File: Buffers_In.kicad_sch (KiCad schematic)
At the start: 19 parts, among them U3 MCP6002-xSN, X1 PEDAL_COMBO_TOP

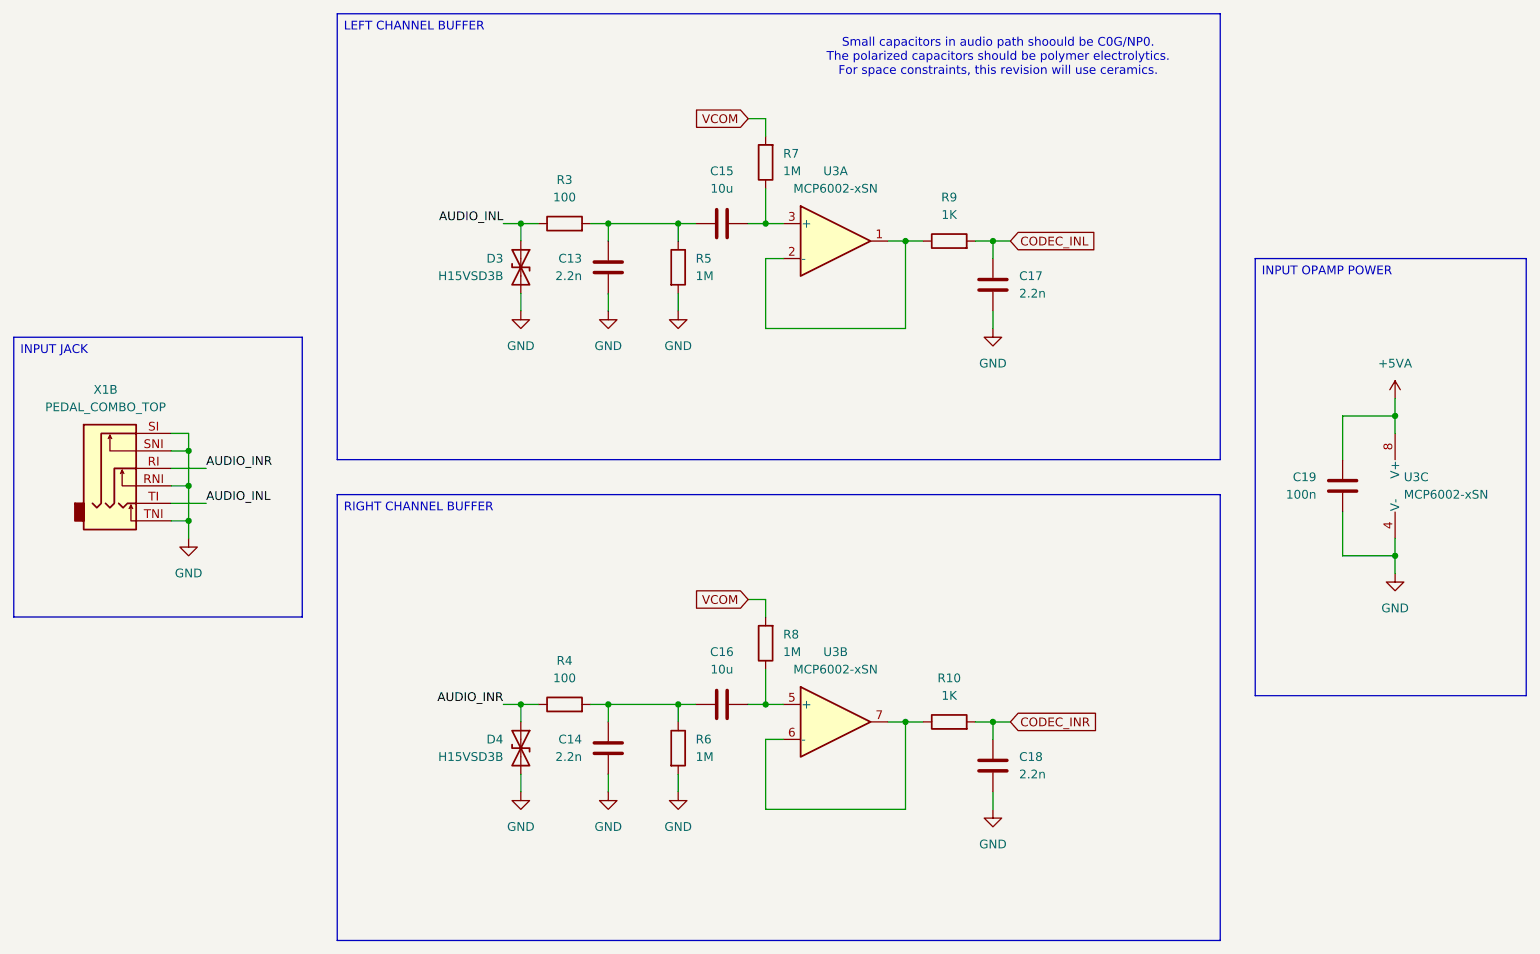
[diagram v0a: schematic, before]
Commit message: Input buffer and power
Updated the input buffer layout.
Updated the power supply layout.
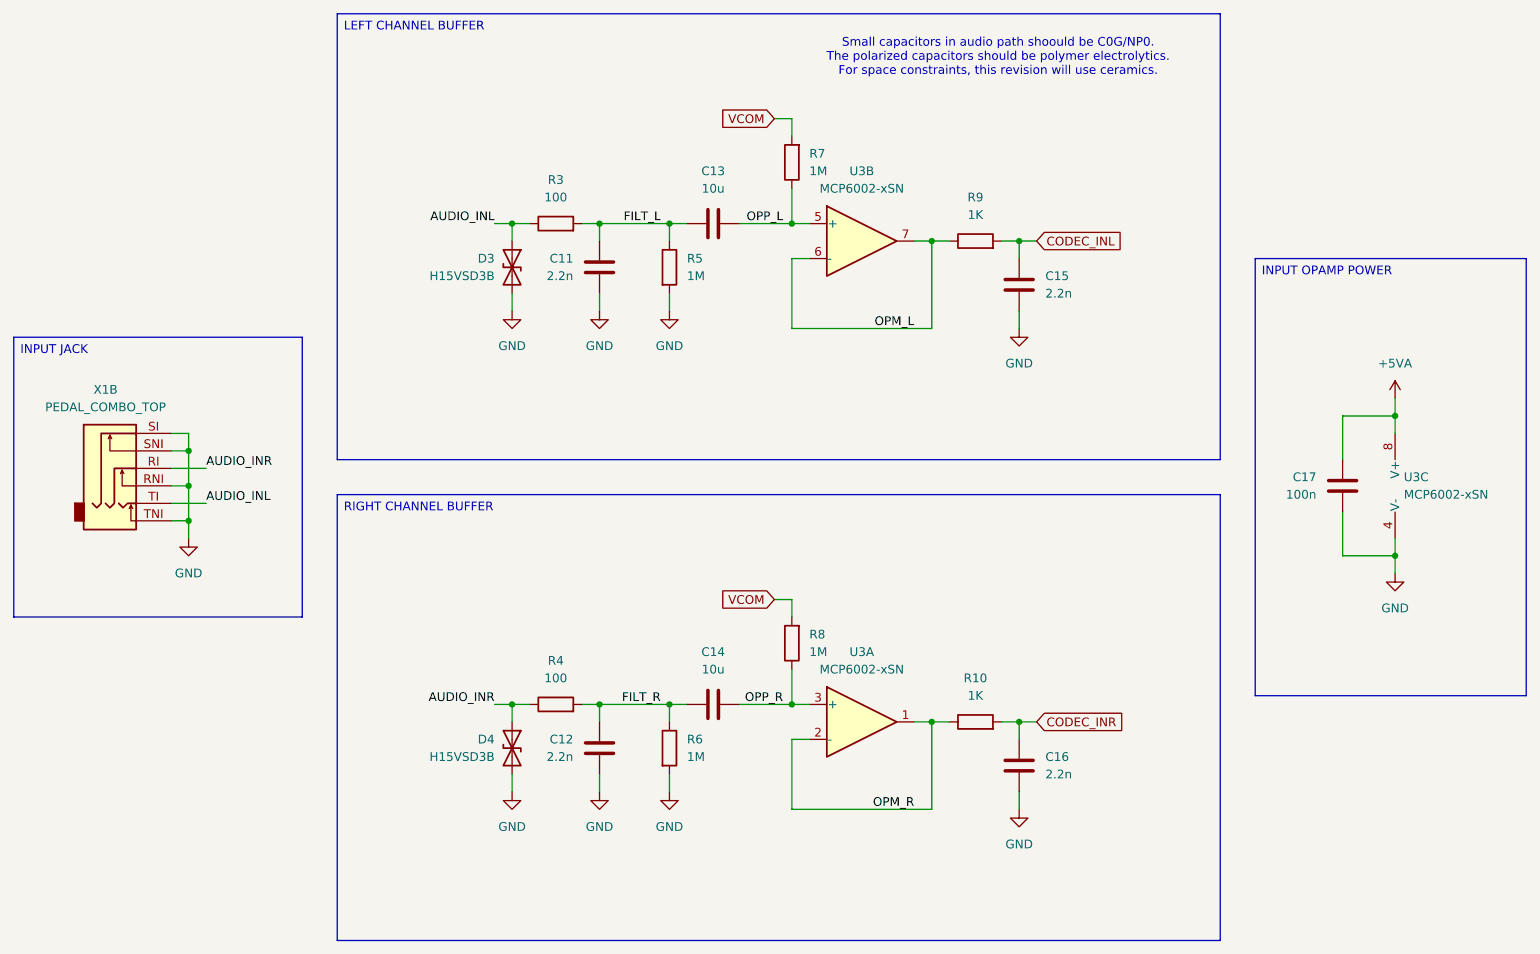
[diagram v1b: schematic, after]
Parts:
- C13: renamed from C15; footprint Capacitor_SMD:C_1206_3216Metric -> Capacitor_SMD:C_0805_2012Metric
- C14: renamed from C16; footprint Capacitor_SMD:C_1206_3216Metric -> Capacitor_SMD:C_0805_2012Metric
- renumbered C13 to C11, C14 to C12, C17 to C15, C18 to C16, C19 to C17
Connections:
- net FILT_R: now reaches C12.2, C14.1, R4.2, R6.1
- net OPM_L: now reaches U3.6 (-), U3.7
- net OPM_L: now also R9.1; no longer R10.1
- net OPM_R: now reaches U3.1, U3.2 (-)
- net OPM_R: now also R10.1; no longer R9.1
- net OPP_L: now reaches C13.2, R7.1
- net OPP_L: now also U3.5 (+); no longer U3.3 (+)
- net FILT_L: now reaches C11.2, C13.1, R3.2, R5.1
- net OPP_R: now reaches C14.2, R8.1
- net OPP_R: now also U3.3 (+); no longer U3.5 (+)
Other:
- moved on the sheet: C11, C12, C13, C14, C15, C16, D3, D4, R10, R3, R4, R5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

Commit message: Codec layout
Updated the codec layout.
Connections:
- net AUDIO_INL: now also R4.1; no longer R3.1
- net AUDIO_INR: now also R3.1; no longer R4.1
- net CODEC_INL: now also C16.1, R10.2; no longer C15.1, R9.2
- net CODEC_INR: now also C15.1, R9.2; no longer C16.1, R10.2
- net FILT_L: now also C12.2, C14.1, R4.2, R6.1; no longer C11.2, C13.1, R3.2, R5.1
- net FILT_R: now also C11.2, C13.1, R3.2, R5.1; no longer C12.2, C14.1, R4.2, R6.1
- net OPM_L: now also R10.1, U3.1, U3.2 (-); no longer R9.1, U3.6 (-), U3.7
- net OPM_R: now also R9.1, U3.6 (-), U3.7; no longer R10.1, U3.1, U3.2 (-)
- net OPP_L: now also C14.2, R8.1, U3.3 (+); no longer C13.2, R7.1, U3.5 (+)
- net OPP_R: now also C13.2, R7.1, U3.5 (+); no longer C14.2, R8.1, U3.3 (+)
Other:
- moved on the sheet: C11, C12, C13, C14, C15, C16, R10, R3, R4, R5, R6, R7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

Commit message: Missing connections
Updated the board layout.
Added al missing connections.
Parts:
- renumbered C12 to C11, C11 to C12, C14 to C13, C13 to C14, C16 to C15, C15 to C16, R9 to R10, R4 to R3, R3 to R4, R6 to R5, R5 to R6, R8 to R7, R7 to R8, R10 to R9
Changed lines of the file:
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@@
 		(on_board yes)
 		(dnp no)
-		(property "Reference" "C12"
+		(property "Reference" "C11"
 			(at 118.11 57.1501 0)
 			(effects
@@
 			(project "SimpleCodec"
 				(path "/4cbf131b-42e8-4a05-beea-68c6d66cdb1a/469e8ad1-854f-4ea5-8b66-be90c8cb100f"
-					(reference "C12")
+					(reference "C11")
 					(unit 1)
 				)
@@
 		(dnp no)
 		(fields_autoplaced yes)
-		(property "Reference" "R10"
+		(property "Reference" "R9"
 			(at 176.53 48.26 90)
 			(effects
@@
 			(project "SimpleCodec"
 				(path "/4cbf131b-42e8-4a05-beea-68c6d66cdb1a/469e8ad1-854f-4ea5-8b66-be90c8cb100f"
-					(reference "R10")
+					(reference "R9")
 					(unit 1)
 				)
@@
 		(dnp no)
 		(fields_autoplaced yes)
-		(property "Reference" "R6"
+		(property "Reference" "R5"
 			(at 134.62 57.1499 0)
 			(effects
@@
 			(project "SimpleCodec"
 				(path "/4cbf131b-42e8-4a05-beea-68c6d66cdb1a/469e8ad1-854f-4ea5-8b66-be90c8cb100f"
-					(reference "R6")
+					(reference "R5")
 					(unit 1)
 				)
@@
 		(dnp no)
 		(fields_autoplaced yes)
-		(property "Reference" "R9"
+		(property "Reference" "R10"
 			(at 176.53 118.11 90)
 			(effects
@@
 			(project "SimpleCodec"
 				(path "/4cbf131b-42e8-4a05-beea-68c6d66cdb1a/469e8ad1-854f-4ea5-8b66-be90c8cb100f"
-					(reference "R9")
+					(reference "R10")
 					(unit 1)
 				)
@@
 		(dnp no)
 		(fields_autoplaced yes)
-		(property "Reference" "C16"
+		(property "Reference" "C15"
 			(at 186.69 59.6899 0)
 			(effects
@@
 			(project "SimpleCodec"
 				(path "/4cbf131b-42e8-4a05-beea-68c6d66cdb1a/469e8ad1-854f-4ea5-8b66-be90c8cb100f"
-					(reference "C16")
+					(reference "C15")
 					(unit 1)
 				)
@@
 		(dnp no)
 		(fields_autoplaced yes)
-		(property "Reference" "R5"
+		(property "Reference" "R6"
 			(at 134.62 126.9999 0)
 			(effects
@@
 			(project "SimpleCodec"
 				(path "/4cbf131b-42e8-4a05-beea-68c6d66cdb1a/469e8ad1-854f-4ea5-8b66-be90c8cb100f"
-					(reference "R5")
+					(reference "R6")
 					(unit 1)
 				)
@@
 		(on_board yes)
 		(dnp no)
-		(property "Reference" "C11"
+		(property "Reference" "C12"
 			(at 118.11 127.0001 0)
 			(effects
@@
 			(project "SimpleCodec"
 				(path "/4cbf131b-42e8-4a05-beea-68c6d66cdb1a/469e8ad1-854f-4ea5-8b66-be90c8cb100f"
-					(reference "C11")
+					(reference "C12")
 					(unit 1)
 				)
@@
 		(dnp no)
 		(fields_autoplaced yes)
-		(property "Reference" "C15"
+		(property "Reference" "C16"
 			(at 186.69 129.5399 0)
 			(effects
@@
 			(project "SimpleCodec"
 				(path "/4cbf131b-42e8-4a05-beea-68c6d66cdb1a/469e8ad1-854f-4ea5-8b66-be90c8cb100f"
-					(reference "C15")
+					(reference "C16")
 					(unit 1)
 				)
@@
 		(dnp no)
 		(fields_autoplaced yes)
-		(property "Reference" "R7"
+		(property "Reference" "R8"
 			(at 152.4 111.7599 0)
 			(effects
@@
 			(project "SimpleCodec"
 				(path "/4cbf131b-42e8-4a05-beea-68c6d66cdb1a/469e8ad1-854f-4ea5-8b66-be90c8cb100f"
-					(reference "R7")
+					(reference "R8")
 					(unit 1)
 				)
@@
 		(dnp no)
 		(fields_autoplaced yes)
-		(property "Reference" "C13"
+		(property "Reference" "C14"
 			(at 138.43 114.3 90)
 			(effects
@@
 			(project "SimpleCodec"
 				(path "/4cbf131b-42e8-4a05-beea-68c6d66cdb1a/469e8ad1-854f-4ea5-8b66-be90c8cb100f"
-					(reference "C13")
+					(reference "C14")
 					(unit 1)
 				)
@@
 		(dnp no)
 		(fields_autoplaced yes)
-		(property "Reference" "R3"
+		(property "Reference" "R4"
 			(at 115.57 115.57 90)
 			(effects
@@
 			(project "SimpleCodec"
 				(path "/4cbf131b-42e8-4a05-beea-68c6d66cdb1a/469e8ad1-854f-4ea5-8b66-be90c8cb100f"
-					(reference "R3")
+					(reference "R4")
 					(unit 1)
 				)
@@
 		(dnp no)
 		(fields_autoplaced yes)
-		(property "Reference" "R8"
+		(property "Reference" "R7"
 			(at 152.4 41.9099 0)
 			(effects
@@
 			(project "SimpleCodec"
 				(path "/4cbf131b-42e8-4a05-beea-68c6d66cdb1a/469e8ad1-854f-4ea5-8b66-be90c8cb100f"
-					(reference "R8")
+					(reference "R7")
 					(unit 1)
 				)
@@
 		(dnp no)
 		(fields_autoplaced yes)
-		(property "Reference" "R4"
+		(property "Reference" "R3"
 			(at 115.57 45.72 90)
 			(effects
@@
 			(project "SimpleCodec"
 				(path "/4cbf131b-42e8-4a05-beea-68c6d66cdb1a/469e8ad1-854f-4ea5-8b66-be90c8cb100f"
-					(reference "R4")
+					(reference "R3")
 					(unit 1)
 				)
@@
 		(dnp no)
 		(fields_autoplaced yes)
-		(property "Reference" "C14"
+		(property "Reference" "C13"
 			(at 138.43 44.45 90)
 			(effects
@@
 			(project "SimpleCodec"
 				(path "/4cbf131b-42e8-4a05-beea-68c6d66cdb1a/469e8ad1-854f-4ea5-8b66-be90c8cb100f"
-					(reference "C14")
-					(unit 1)
-				)
+					(reference "C13")
+					(unit 1)
+				)
